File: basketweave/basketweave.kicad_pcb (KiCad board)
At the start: 2 copper layers, 371.5 x 145.3 mm, 177 parts, among them U1 ATmega32A-PU, Y1 16Mhz

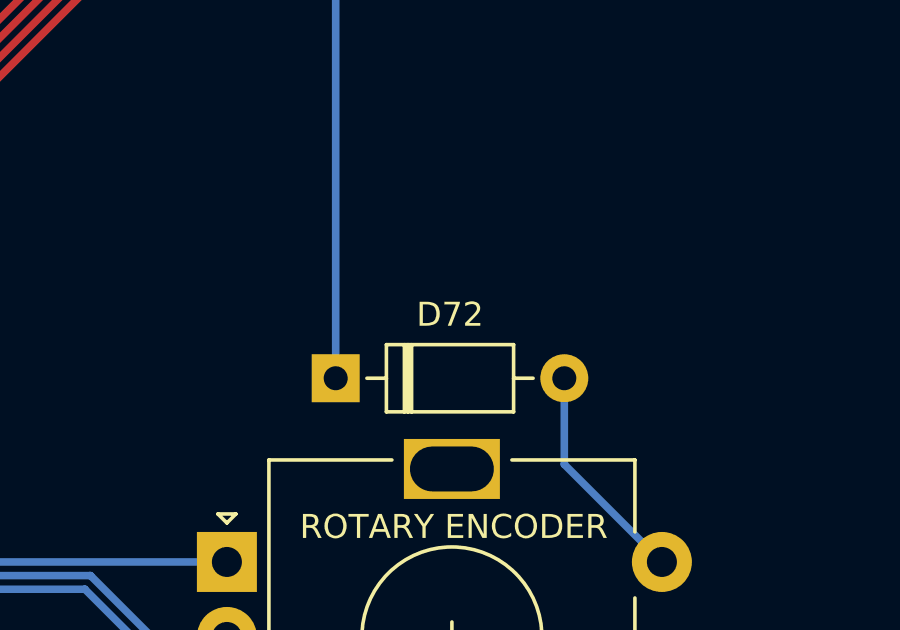
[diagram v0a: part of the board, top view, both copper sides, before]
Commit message: fixed inaccurate label
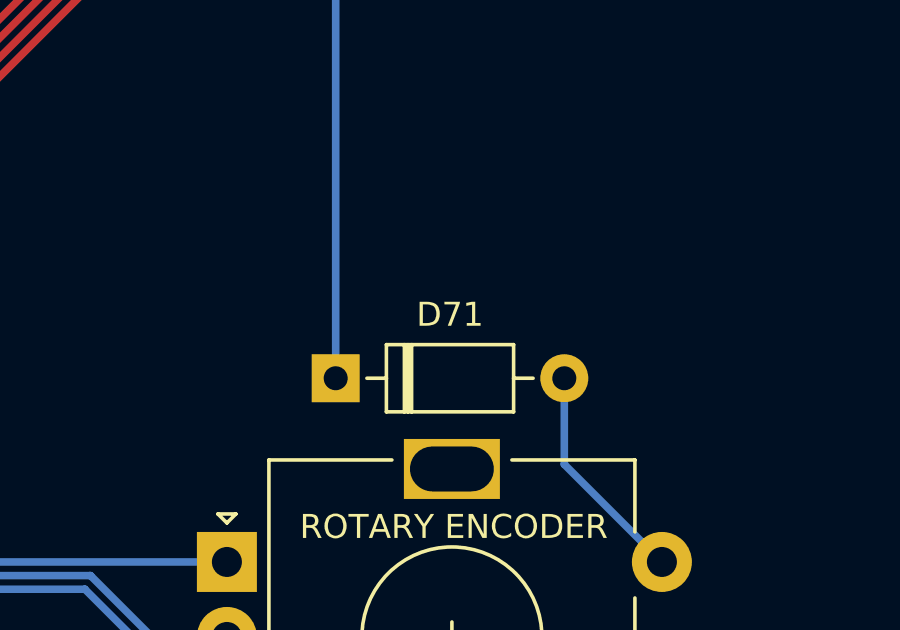
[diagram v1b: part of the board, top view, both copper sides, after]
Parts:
- renumbered D72 to D71
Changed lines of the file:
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@@
     (descr "Diode, DO-35_SOD27 series, Axial, Horizontal, pin pitch=7.62mm, , length*diameter=4*2mm^2, , http://www.diodes.com/_files/packages/DO-35.pdf")
     (tags "Diode DO-35_SOD27 series Axial Horizontal pin pitch 7.62mm  length 4mm diameter 2mm")
-    (fp_text reference D72 (at 3.81 -2.12) (layer F.SilkS)
+    (fp_text reference D71 (at 3.81 -2.12) (layer F.SilkS)
       (effects (font (size 0.8 0.8) (thickness 0.15)))
     )
